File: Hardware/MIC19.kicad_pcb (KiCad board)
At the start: 2 copper layers, 160 x 70 mm, 72 parts, among them J101 ENGINE_VEL, J102 ENGINE_ACEL, J103 MPPT_POT, J104 SW_PUMP1_ON, J105 SW_PUMP2_ON, J106 SW_PUMP3_ON, J107 SW_BOAT_ON, J108 SW_ENGINE_ON, J109 SW_MPPT_ON, J110 SW_DMS, J111 SW_EMERGENCIA, J401 USART, J601 RJ45, J602 RJ45, Q101 BCV27, U201 MCP2551-I/SN, U202 MCP2515-xSO, U401 ATMEGA328P-PU, U501 LM7805, Y201 16MHz, Y401 16MHz

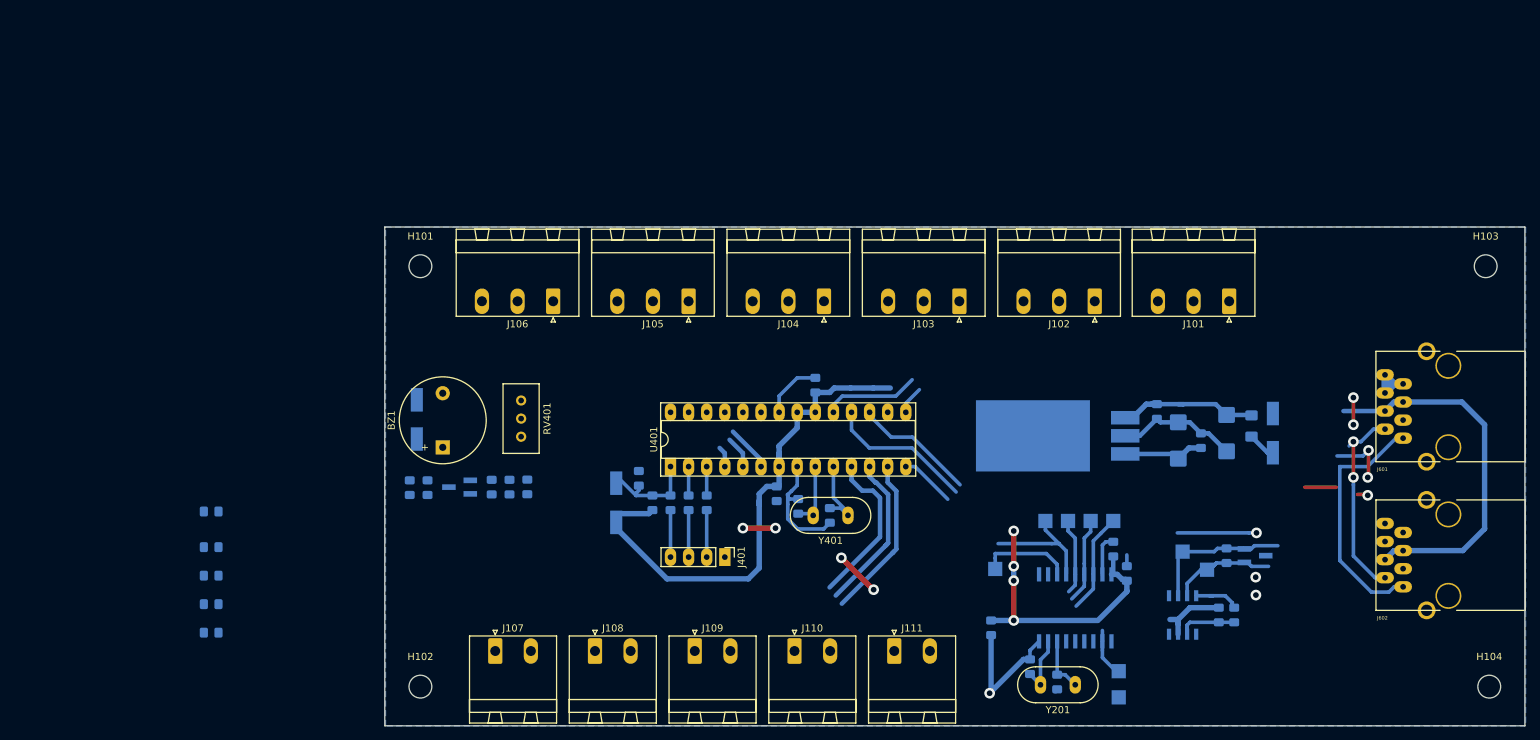
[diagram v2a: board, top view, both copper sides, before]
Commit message: Modificaçoes nos resistores pull-up e modificaçoes no layout
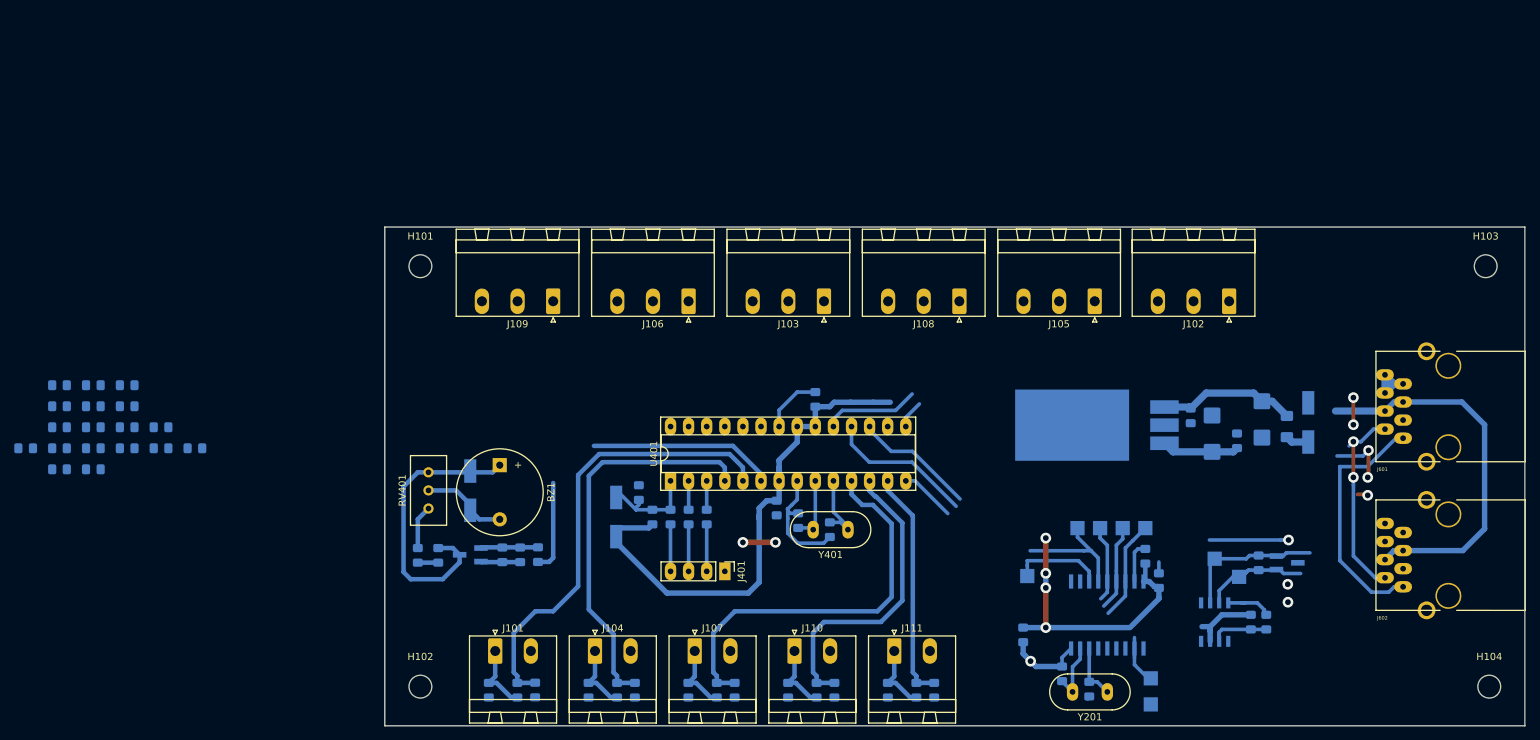
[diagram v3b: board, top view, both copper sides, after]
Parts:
- added C101: 100n, Capacitor_SMD:C_0805_2012Metric_Pad1.15x1.40mm_HandSolder, B.Cu at (73.0, 134.1)
- added C102: 100n, Capacitor_SMD:C_0805_2012Metric_Pad1.15x1.40mm_HandSolder, B.Cu at (1.47, 100.1)
- added C103: 100n, Capacitor_SMD:C_0805_2012Metric_Pad1.15x1.40mm_HandSolder, B.Cu at (6.22, 103.1)
- added C104: 100n, Capacitor_SMD:C_0805_2012Metric_Pad1.15x1.40mm_HandSolder, B.Cu at (87.0, 134.1)
- added C105: 100n, Capacitor_SMD:C_0805_2012Metric_Pad1.15x1.40mm_HandSolder, B.Cu at (6.22, 100.1)
- added C106: 100n, Capacitor_SMD:C_0805_2012Metric_Pad1.15x1.40mm_HandSolder, B.Cu at (11.0, 103.1)
- added C107: 100n, Capacitor_SMD:C_0805_2012Metric_Pad1.15x1.40mm_HandSolder, B.Cu at (101.0, 134.1)
- added C108: 100n, Capacitor_SMD:C_0805_2012Metric_Pad1.15x1.40mm_HandSolder, B.Cu at (6.22, 97.2)
- added C109: 100n, Capacitor_SMD:C_0805_2012Metric_Pad1.15x1.40mm_HandSolder, B.Cu at (11.0, 100.1)
- added C110: 100n, Capacitor_SMD:C_0805_2012Metric_Pad1.15x1.40mm_HandSolder, B.Cu at (115.0, 134.1)
- added C111: 100n, Capacitor_SMD:C_0805_2012Metric_Pad1.15x1.40mm_HandSolder, B.Cu at (129.0, 134.1)
- added R106: 100R, Resistor_SMD:R_0805_2012Metric_Pad1.15x1.40mm_HandSolder, B.Cu at (6.22, 91.3)
- added R107: 10k, Resistor_SMD:R_0805_2012Metric_Pad1.15x1.40mm_HandSolder, B.Cu at (80.5, 134.1)
- added R108: 10k, Resistor_SMD:R_0805_2012Metric_Pad1.15x1.40mm_HandSolder, B.Cu at (11.0, 94.2)
- added R109: 10k, Resistor_SMD:R_0805_2012Metric_Pad1.15x1.40mm_HandSolder, B.Cu at (15.7, 97.2)
- added R110: 100R, Resistor_SMD:R_0805_2012Metric_Pad1.15x1.40mm_HandSolder, B.Cu at (84.5, 134.1)
- added R111: 100R, Resistor_SMD:R_0805_2012Metric_Pad1.15x1.40mm_HandSolder, B.Cu at (20.5, 100.1)
- added R112: 100R, Resistor_SMD:R_0805_2012Metric_Pad1.15x1.40mm_HandSolder, B.Cu at (11.0, 91.3)
- added R113: 10k, Resistor_SMD:R_0805_2012Metric_Pad1.15x1.40mm_HandSolder, B.Cu at (94.5, 134.1)
- added R114: 10k, Resistor_SMD:R_0805_2012Metric_Pad1.15x1.40mm_HandSolder, B.Cu at (15.7, 94.2)
- added R115: 10k, Resistor_SMD:R_0805_2012Metric_Pad1.15x1.40mm_HandSolder, B.Cu at (20.5, 97.2)
- added R116: 100R, Resistor_SMD:R_0805_2012Metric_Pad1.15x1.40mm_HandSolder, B.Cu at (98.5, 134.1)
- added R117: 100R, Resistor_SMD:R_0805_2012Metric_Pad1.15x1.40mm_HandSolder, B.Cu at (25.2, 100.1)
- added R118: 100R, Resistor_SMD:R_0805_2012Metric_Pad1.15x1.40mm_HandSolder, B.Cu at (15.7, 91.3)
- added R119: 10k, Resistor_SMD:R_0805_2012Metric_Pad1.15x1.40mm_HandSolder, B.Cu at (108.5, 134.1)
- added R120: 100R, Resistor_SMD:R_0805_2012Metric_Pad1.15x1.40mm_HandSolder, B.Cu at (112.5, 134.1)
- added R121: 10k, Resistor_SMD:R_0805_2012Metric_Pad1.15x1.40mm_HandSolder, B.Cu at (122.5, 134.1)
- added R122: 100R, Resistor_SMD:R_0805_2012Metric_Pad1.15x1.40mm_HandSolder, B.Cu at (126.5, 134.1)
- R101, R102, R103: value 1k -> 10k
- R104, R105: value 1k -> 100R
- moved R104 49.7 mm to (70.5, 134.1), turned to 90 degrees
- moved R101 42.2 mm to (66.5, 134.1), turned to 90 degrees
- moved R103 33.2 mm to (11.0, 97.2)
- moved R102 29.1 mm to (6.22, 94.2)
- moved R105 24.8 mm to (15.7, 100.1)
- moved RV401 13.9 mm to (58.0, 103.5), turned to 90 degrees
- moved D402 12.5 mm to (63.9, 106.1), turned to 90 degrees
- moved D403 10.3 mm to (59.4, 115.2)
- moved C407 9.62 mm to (68.4, 115.1)
- moved Q101 9.62 mm to (63.9, 115.1)
- moved R404 9.62 mm to (73.4, 115.1)
- moved R405 9.62 mm to (70.9, 115.1)
- moved R406 9.60 mm to (56.5, 115.2)
- moved BZ1 8.38 mm to (68.0, 102.5), turned to 270 degrees
- moved U501 5.70 mm to (160.0, 94.3)
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- renumbered J107 to J101, J101 to J102, J104 to J103, J108 to J104, J102 to J105, J105 to J106, J109 to J107, J103 to J108, J106 to J109
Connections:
- J101 pad 1: GND -> Net-(J101-Pad1)
- J101 pad 2: /Conectores/SW_BOAT_ON -> GND
- J102 pad 1: GND -> +5V
- J102 pad 2: /Conectores/ENGINE_VEL -> Net-(J102-Pad2)
- J102 pad 3: +5V -> GND
- J103 pad 1: GND -> +5V
- J103 pad 2: /Conectores/SW_PUMP1_ON -> Net-(J103-Pad2)
- J103 pad 3: +5V -> GND
- J104 pad 1: GND -> Net-(J104-Pad1)
- J104 pad 2: /Conectores/SW_ENGINE_ON -> GND
- J105 pad 1: GND -> +5V
- J105 pad 2: /Conectores/ENGINE_ACEL -> Net-(J105-Pad2)
- J105 pad 3: +5V -> GND
- J106 pad 1: GND -> +5V
- J106 pad 2: /Conectores/SW_PUMP2_ON -> Net-(J106-Pad2)
- J106 pad 3: +5V -> GND
- J107 pad 1: GND -> Net-(J107-Pad1)
- J107 pad 2: /Conectores/SW_MPPT_ON -> GND
- J108 pad 1: GND -> +5V
- J108 pad 2: /Conectores/MPPT_POT -> Net-(J108-Pad2)
- J108 pad 3: +5V -> GND
- J109 pad 1: GND -> +5V
- J109 pad 2: /Conectores/SW_PUMP3_ON -> Net-(J109-Pad2)
- J109 pad 3: +5V -> GND
- J110 pad 1: GND -> Net-(J110-Pad1)
- J110 pad 2: /Conectores/SW_DMS -> GND
- J111 pad 1: GND -> Net-(J111-Pad1)
- J111 pad 2: /Conectores/SW_EMERGENCIA -> GND
- R101 pad 2: /Conectores/SW_BOAT_ON -> Net-(J101-Pad1)
- R102 pad 2: /Conectores/SW_ENGINE_ON -> Net-(J102-Pad2)
- R103 pad 2: /Conectores/SW_MPPT_ON -> Net-(J103-Pad2)
- R104 pad 1: +5V -> Net-(J101-Pad1)
- R104 pad 2: /Conectores/SW_DMS -> /Conectores/SW_ENGINE_ON
- R105 pad 1: +5V -> Net-(J102-Pad2)
- R105 pad 2: /Conectores/SW_EMERGENCIA -> /Conectores/ENGINE_VEL
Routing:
- net /Conectores/SW_ENGINE_ON: track 4.99 -> 64.5 mm
- net /Conectores/SW_MPPT_ON: track 2.92 -> 55.3 mm
- net Net-(BZ1-Pad1): track 0.00 -> 40.5 mm
- net /Conectores/SW_BOAT_ON: track 23.3 -> 57.2 mm
- net /MCU/BUZZER: track 6.99 -> 39.4 mm
- net GND: track 122.0 -> 90.7 mm, vias 13 -> 11
- net /Conectores/SW_DMS: track 23.8 -> 43.8 mm
- net Net-(BZ1-Pad2): track 0.00 -> 12.2 mm
- net Net-(J107-Pad1): track 0.00 -> 9.70 mm
- net Net-(J111-Pad1): track 0.00 -> 9.70 mm
- net Net-(J110-Pad1): track 0.00 -> 9.70 mm
- net Net-(J104-Pad1): track 0.00 -> 9.70 mm
- net Net-(J101-Pad1): track 0.00 -> 9.70 mm
- net /Conectores/SW_EMERGENCIA: track 23.4 -> 32.5 mm
- net Net-(C407-Pad2): track 0.00 -> 8.04 mm
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- removed copper zone on B.Cu, net (none)
